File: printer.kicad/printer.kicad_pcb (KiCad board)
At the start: 2 copper layers, 73.7 x 83.8 mm, 35 parts, among them J1 ZX_Spectrum_128K_expansion, J2 Conn_01x08_Male, J3 Conn_01x05_Male, J4 Conn_01x04_Male, U1 SN74AHC373, U2 SN74HCT00, U3 SN74AHCT02, U4 SN74AHC373, U5 XC6206PxxxMR, U6 STM32F103C8Tx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

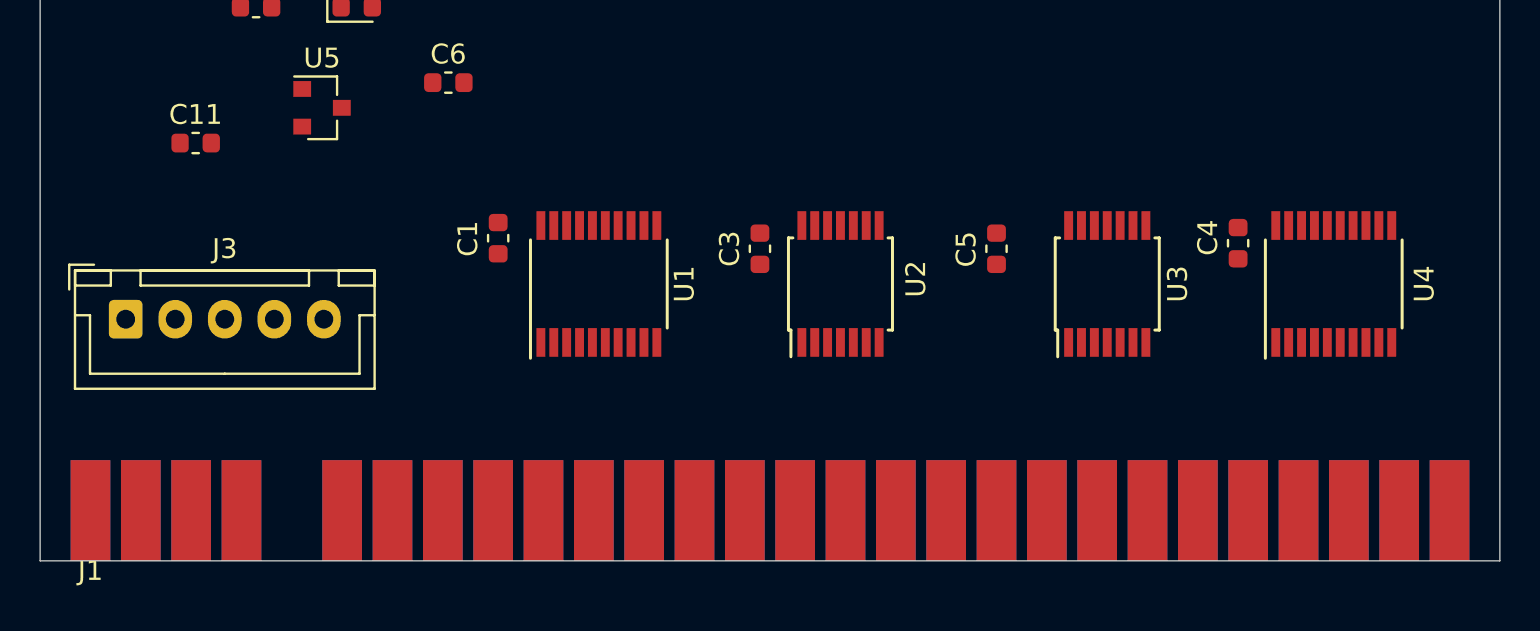
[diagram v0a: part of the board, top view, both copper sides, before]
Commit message: Route all bus signal pins and some chip connections
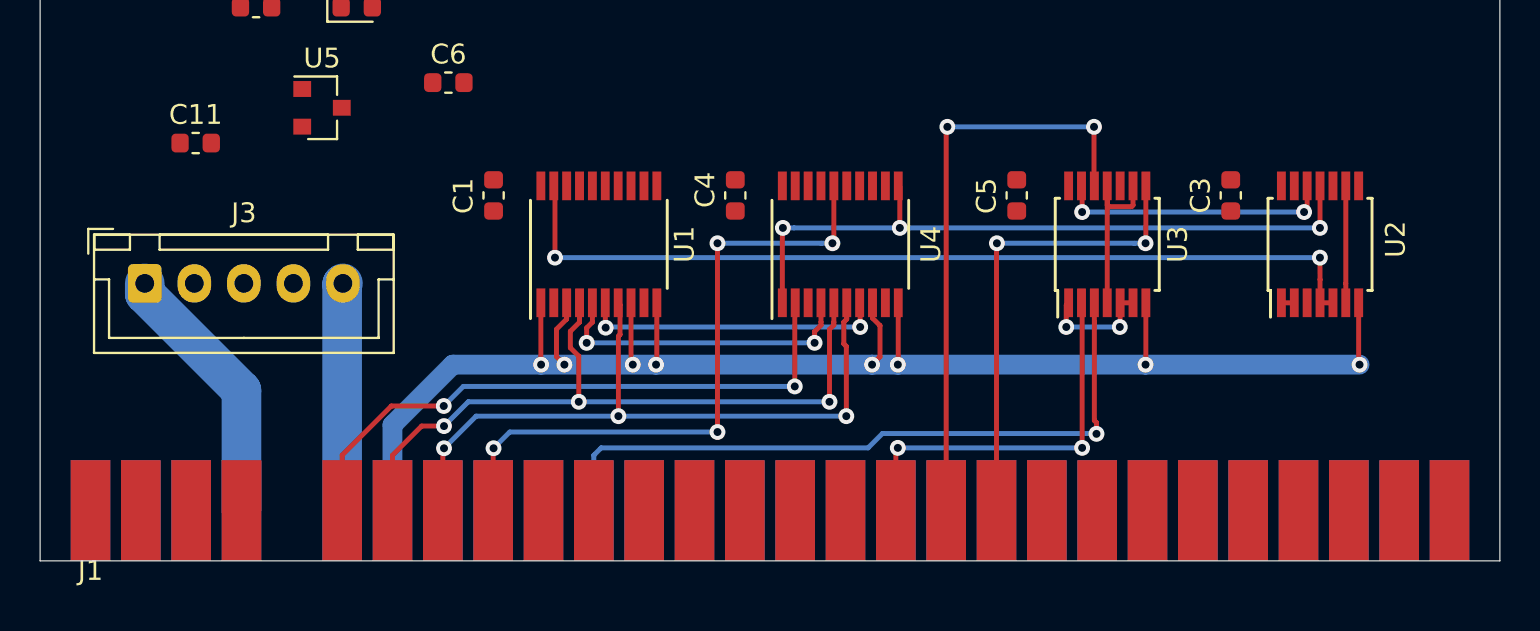
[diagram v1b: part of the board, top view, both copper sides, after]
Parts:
- moved C4 25.5 mm to (144.3, 108.6)
- moved U4 25.0 mm to (149.6, 111.0)
- moved U2 24.3 mm to (173.8, 111.0)
- moved C3 23.9 mm to (169.3, 108.6)
- moved C5 2.88 mm to (158.5, 108.6)
- moved C1 2.17 mm to (132.1, 108.6)
- moved J3 2.05 mm to (114.5, 113.0)
- moved U1 2.00 mm to (137.4, 111.0)
- moved U3 2.00 mm to (163.1, 111.0)
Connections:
- J1 pad a14: GND -> Net-(J1-Pada14)
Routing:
- net GND: track 0.00 -> 91.6 mm, vias 0 -> 8
- net /STYLUS: track 0.00 -> 45.2 mm, vias 0 -> 2
- net /D1: track 0.00 -> 36.4 mm, vias 0 -> 3
- net /D2: track 0.00 -> 35.8 mm, vias 0 -> 3
- net /A2: track 0.00 -> 35.3 mm, vias 0 -> 1
- net Net-(U2-Pad11): track 0.00 -> 35.2 mm, vias 0 -> 3
- net /D6: track 0.00 -> 33.0 mm, vias 0 -> 4
- net /D0: track 0.00 -> 31.3 mm, vias 0 -> 2
- net /~RD: track 0.00 -> 29.8 mm, vias 0 -> 2
- net /~WR: track 0.00 -> 23.9 mm, vias 0 -> 2
- net /~IORQ: track 0.00 -> 19.8 mm, vias 0 -> 2
- net /MOTOR_SLOW: track 0.00 -> 15.8 mm, vias 0 -> 2
- net /MOTOR_OFF: track 0.00 -> 15.4 mm, vias 0 -> 2
- net /READ: track 0.00 -> 13.9 mm, vias 0 -> 2
- net +9V: track 0.00 -> 13.5 mm
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
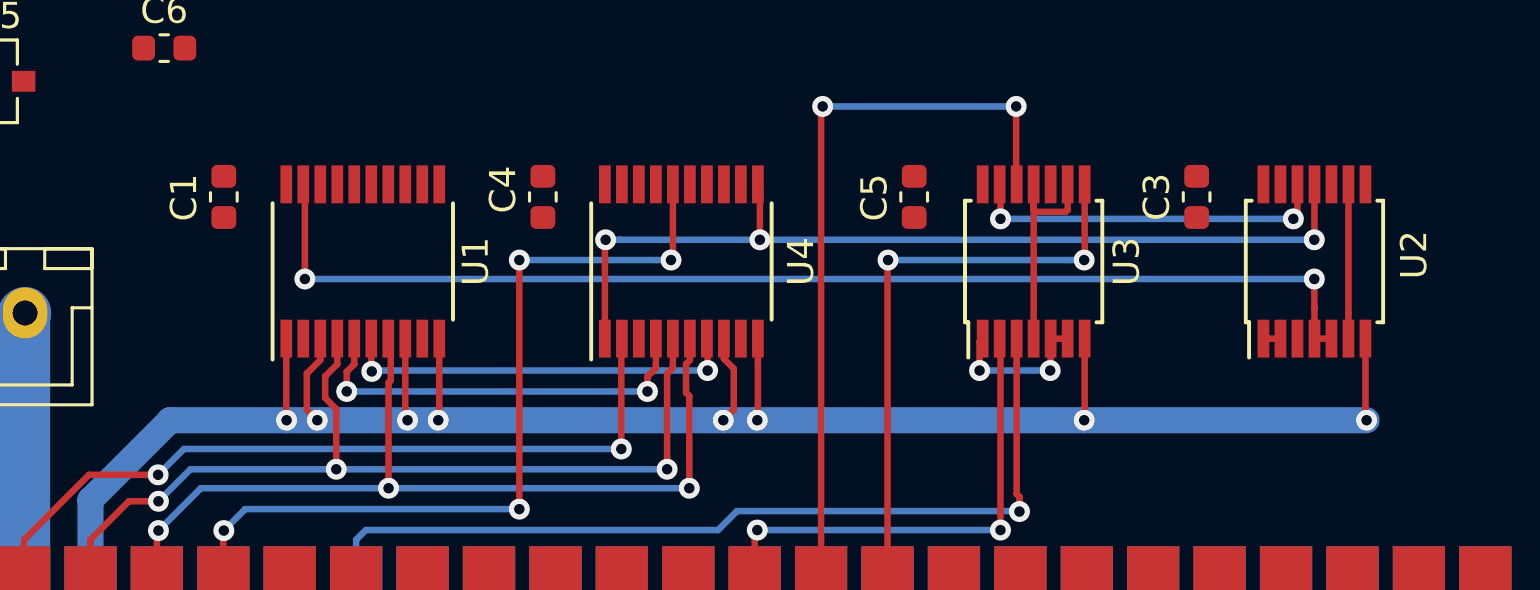
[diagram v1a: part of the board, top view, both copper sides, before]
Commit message: Route all internal connections for interface chips
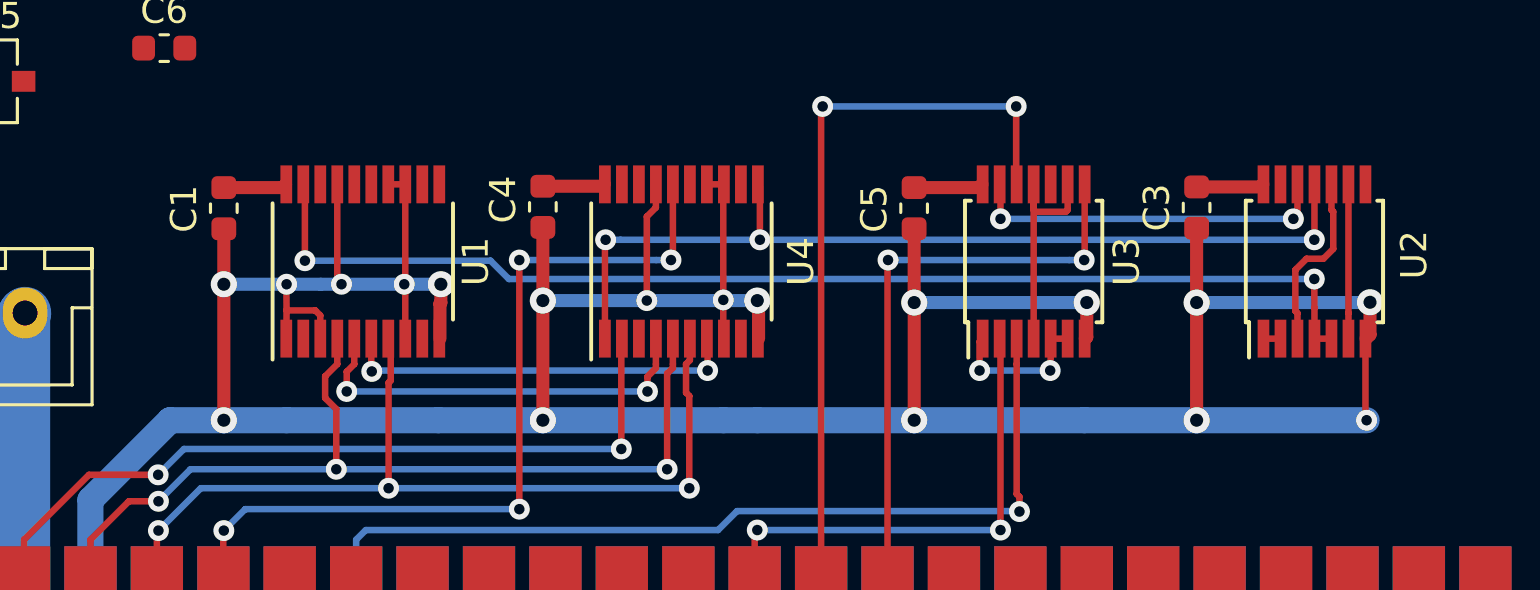
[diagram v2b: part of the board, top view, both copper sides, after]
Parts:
- moved C5 0.43 mm to (158.5, 109.0)
- moved C1 0.43 mm to (132.1, 109.0)
- moved C3 0.41 mm to (169.3, 109.0)
- moved C4 0.38 mm to (144.3, 108.9)
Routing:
- net GND: track 91.6 -> 160.6 mm, vias 8 -> 18
- net +5V: track 0.00 -> 10.0 mm
- net /~PAPER: track 0.00 -> 6.94 mm

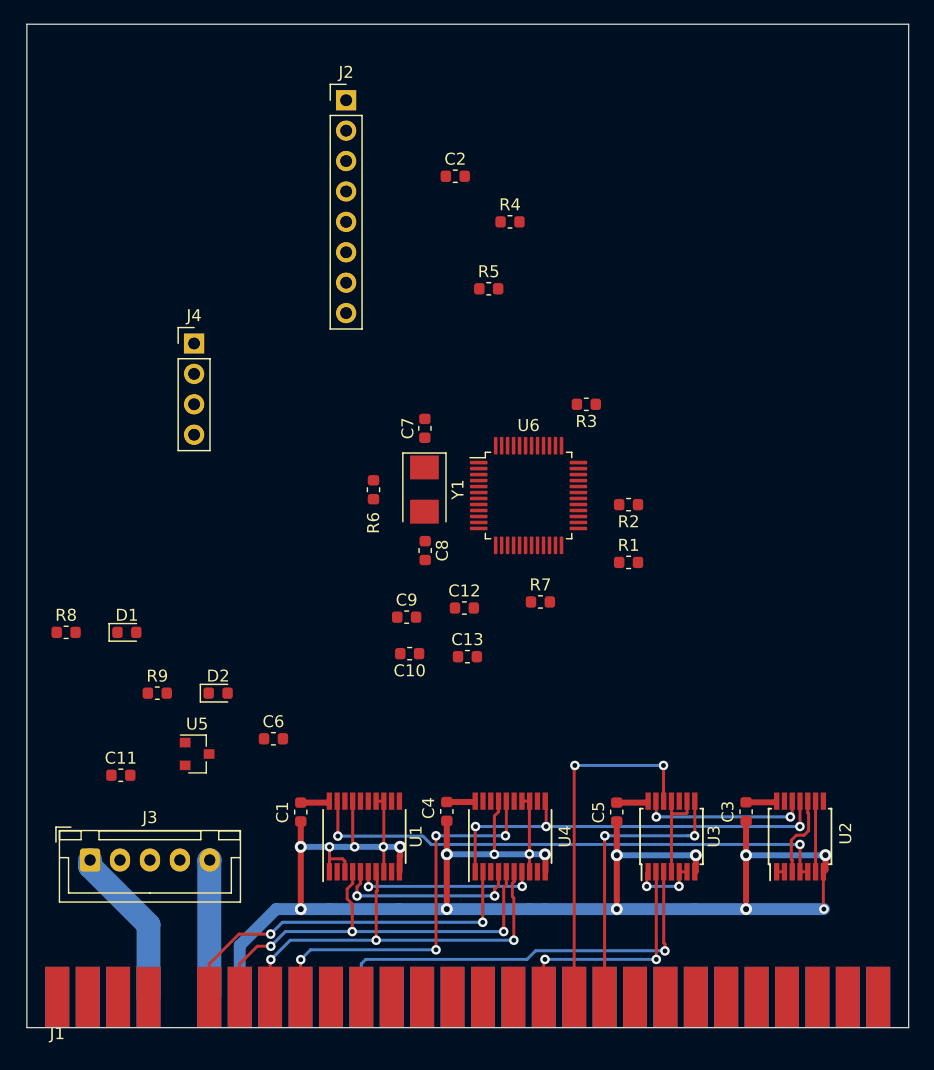
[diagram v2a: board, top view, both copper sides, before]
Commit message: Layout MCU surroundings roughly
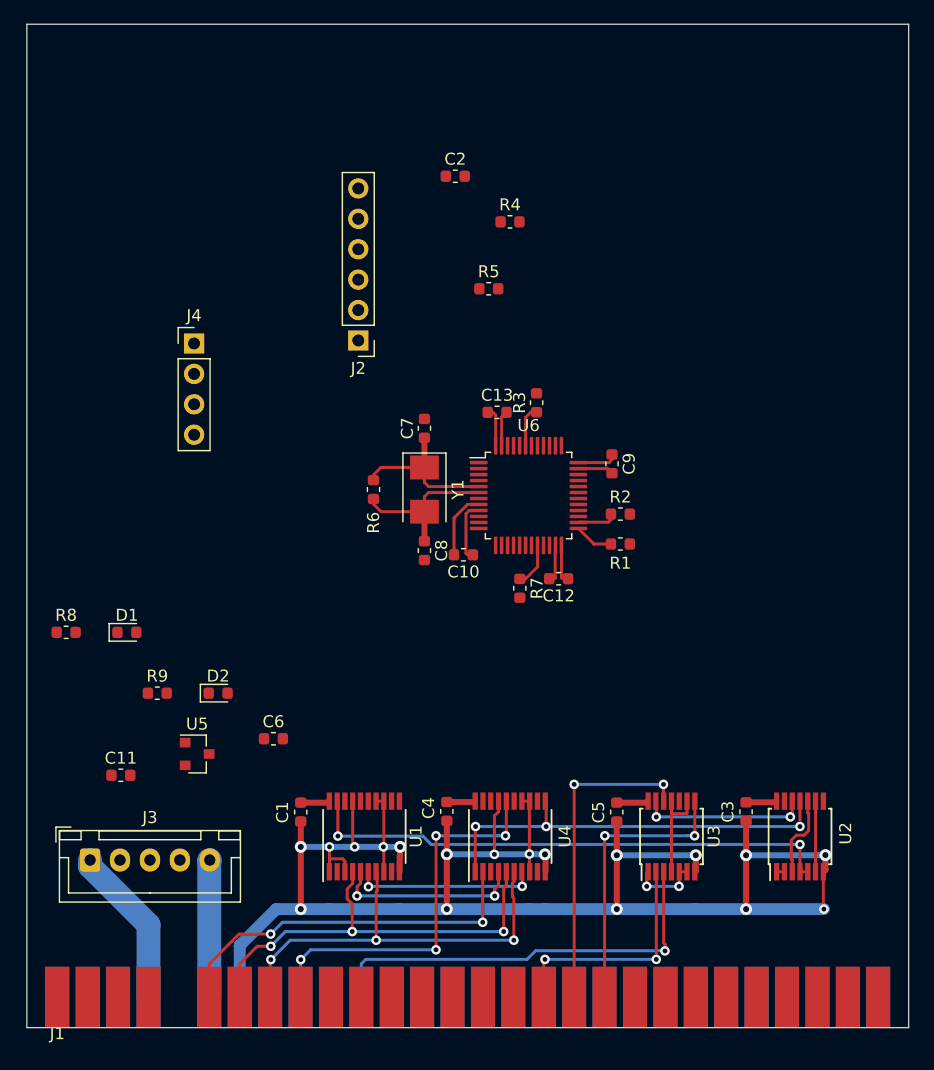
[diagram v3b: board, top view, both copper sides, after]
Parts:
- J2: value Conn_01x08_Male -> Conn_01x06_Male; footprint Connector_PinHeader_2.54mm:PinHeader_1x08_P2.54mm_Vertical -> Connector_PinHeader_2.54mm:PinHeader_1x06_P2.54mm_Vertical
- moved C9 21.4 mm to (158.1, 79.9), turned to 270 degrees
- moved C13 20.6 mm to (148.5, 75.6)
- moved J2 20.1 mm to (136.9, 69.6), turned to 180 degrees
- moved C10 9.40 mm to (145.7, 87.5)
- moved C12 8.25 mm to (153.6, 89.5), turned to 180 degrees
- moved R3 4.16 mm to (151.8, 74.8), turned to 90 degrees
- moved R7 2.06 mm to (150.4, 90.3), turned to 270 degrees
- moved R1 1.68 mm to (158.8, 86.6)
- moved R2 1.05 mm to (158.8, 84.1), turned to 0 degrees
- moved C8 0.06 mm to (142.4, 87.1)
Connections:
- J2 pad 1: GND -> +3V3
- J2 pad 2: /BOOT0 -> /~RESET
- J2 pad 3: /DEBUG_RX -> /PROGRAM_TX
- J2 pad 4: /DEBUG_TX -> /PROGRAM_RX
- J2 pad 5: /PROGRAM_RX -> /BOOT0
- J2 pad 6: /PROGRAM_TX -> GND
- U6 pad 21: /DEBUG_TX -> Net-(U6-Pad21)
- U6 pad 22: /DEBUG_RX -> Net-(U6-Pad22)
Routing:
- net +3V3: track 0.00 -> 15.0 mm
- net GND: track 160.6 -> 175.4 mm
- net /OSC_IN: track 0.00 -> 13.4 mm
- net /OSC_OUT: track 0.00 -> 13.3 mm
- net /BOOT1: track 0.00 -> 3.69 mm
- net /READY: track 0.00 -> 3.46 mm
- net /ENCODER: track 0.00 -> 3.29 mm
- net /PAPER: track 0.65 -> 3.91 mm
- net /~RD: track 29.8 -> 26.7 mm

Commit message: Do most of the layout without ground fill
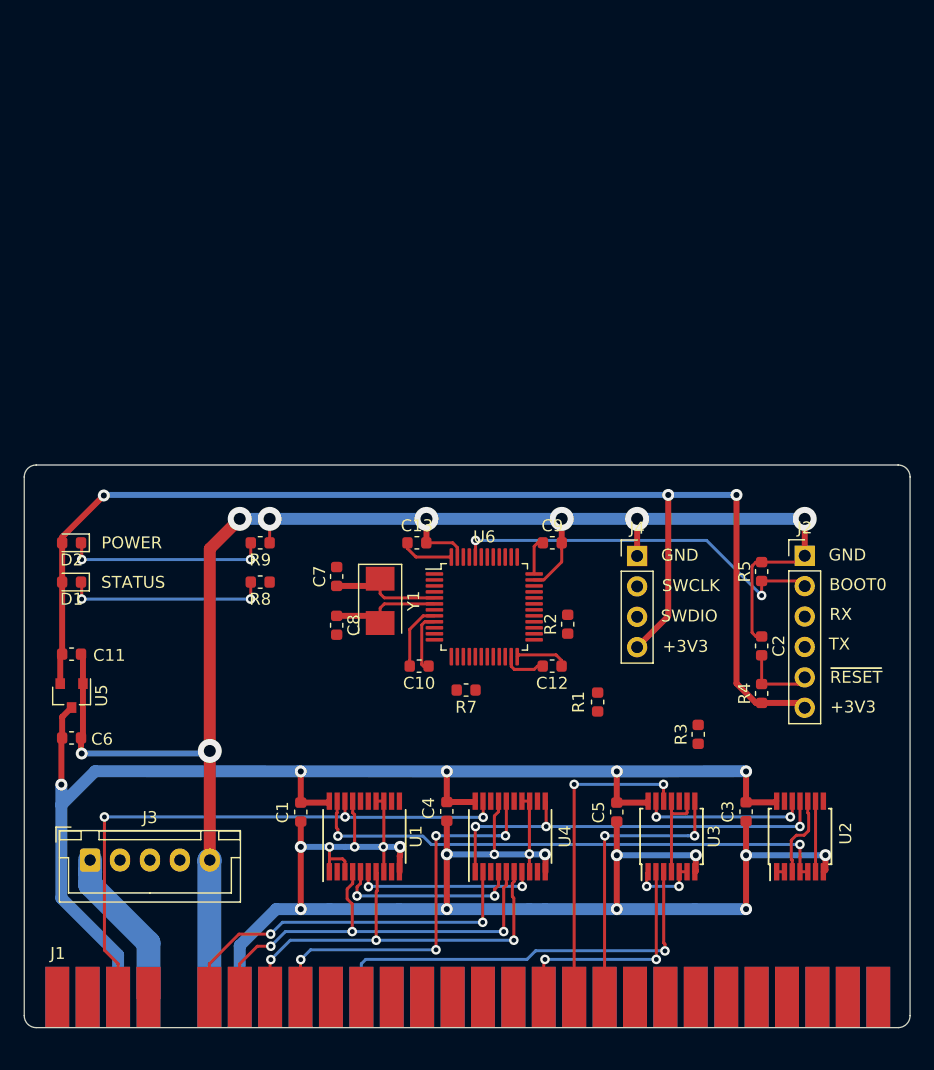
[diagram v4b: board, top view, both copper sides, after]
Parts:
- removed R6: 1M, Resistor_SMD:R_0603_1608Metric
- moved C2 46.8 mm to (170.6, 95.1), turned to 270 degrees
- moved R4 44.7 mm to (170.6, 99.1), turned to 90 degrees
- moved J2 41.4 mm to (174.2, 87.6), turned to 0 degrees
- moved J4 41.0 mm to (160.2, 87.6)
- moved R5 32.8 mm to (170.6, 88.9), turned to 90 degrees
- moved R3 30.8 mm to (165.3, 102.5)
- moved D2 17.5 mm to (113.0, 86.5), turned to 180 degrees
- moved C6 16.9 mm to (113.0, 102.8), turned to 180 degrees
- moved R8 16.8 mm to (128.7, 89.8), turned to 180 degrees
- moved R9 15.2 mm to (128.7, 86.5), turned to 180 degrees
- moved C7 14.4 mm to (135.1, 89.3)
- moved R1 13.3 mm to (156.9, 99.8), turned to 270 degrees
- moved C13 12.8 mm to (141.8, 86.5)
- moved U5 11.6 mm to (113.0, 99.3), turned to 270 degrees
- moved C11 10.9 mm to (113.0, 95.8), turned to 180 degrees
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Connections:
- J2 pad 1: +3V3 -> GND
- J2 pad 2: /~RESET -> /BOOT0
- J2 pad 3: /PROGRAM_TX -> /PROGRAM_RX
- J2 pad 4: /PROGRAM_RX -> /PROGRAM_TX
- J2 pad 5: /BOOT0 -> /~RESET
- J2 pad 6: GND -> +3V3
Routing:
- net GND: track 175.4 -> 287.7 mm, vias 18 -> 25
- net +3V3: track 15.0 -> 123.3 mm, vias 0 -> 3
- net +5V: track 10.0 -> 105.4 mm, vias 0 -> 5
- net /D7: track 0.00 -> 49.9 mm, vias 0 -> 3
- net /BOOT0: track 0.00 -> 32.2 mm, vias 0 -> 2
- net Net-(D1-Pad1): track 0.00 -> 17.0 mm, vias 0 -> 2
- net Net-(D2-Pad1): track 0.00 -> 16.9 mm, vias 0 -> 2
- net /~RESET: track 0.00 -> 6.23 mm
- net /BOOT1: track 3.69 -> 0.00 mm
- net /OSC_IN: track 13.4 -> 9.81 mm
- net /OSC_OUT: track 13.3 -> 9.81 mm
- net /READY: track 3.46 -> 0.00 mm
- net /ENCODER: track 3.29 -> 0.00 mm
- net /PAPER: track 3.91 -> 0.65 mm
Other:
- board size 73.7 x 83.8 mm -> 74 x 47 mm
- board text added: "+3V3"
- board text added: "BOOT0"
- board text added: "GND"
- board text added: "POWER"
- board text added: "RX"
- board text added: "STATUS"
- board text added: "SWCLK"
- board text added: "SWDIO"
- board text added: "TX"
- board text added: "~RESET"
